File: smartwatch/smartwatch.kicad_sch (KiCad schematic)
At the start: 32 parts, among them J1 BAT_CON, J2 DC_CON, J3 PROG_INT, J4 I2C Touch, J5 SPI Display, J6 Power, J7 Micro_SD_Card, SW1 SW_Push, U1 ESP32-WROVER-E, U2 MCP73831-5-OT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

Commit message: updated pcb schematic and design
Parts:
- removed J4: I2C Touch, Connector_Wire_SMD:Wire_Pad_1x02, symbol Connector_Generic:Conn_01x02
- removed J5: SPI Display, Connector_Wire_SMD:Wire_Pad_1x03, symbol Connector_Generic:Conn_01x03
- removed J7: Micro_SD_Card, Connector_Card:microSD_HC_Hirose_DM3D-SF, symbol Connector:Micro_SD_Card
- added J4: Screen, Connector_Wire_SMD:Wire_Pad_1x07, symbol Connector_Generic:Conn_01x07
- added J5: Touch, Connector_Wire_SMD:Wire_Pad_1x04, symbol Connector_Generic:Conn_01x04
- added J8: SD Card, Connector_Wire_SMD:Wire_Pad_1x06, symbol Connector_Generic:Conn_01x06
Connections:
- net 3V3: now also J4.7 (Pin_7), J8.3 (Pin_3)
- net BTN_INP: now also U1.6 (GPIO34/ADC1_CH6); no longer U1.26 (ADC2_CH0/GPIO4)
- net GND: now also J8.5 (Pin_5)
- net SCR_MISO: now also U1.7 (GPIO35/ADC1_CH7), J4.1 (Pin_1); no longer U1.31 (GPIO19)
- net SCR_MOSI: now also J4.2 (Pin_2)
- net SCR_SCLK: now also J4.3 (Pin_3)
- net SD_MISO: now also J8.6 (Pin_6)
- net SD_MOSI: now also J8.2 (Pin_2)
- net SD_SCLK: now also J8.4 (Pin_4)
- net SD_SS: now also U1.12 (ADC2_CH7/GPIO27), J8.1 (Pin_1); no longer U1.23 (MTDO/GPIO15/ADC2_CH3)
- net TOUCH_SCL: now also J5.3 (Pin_3)
- net TOUCH_SDA: now also J5.4 (Pin_4)
- net TOUCH_IRQ: now reaches U1.10 (DAC_1/ADC2_CH8/GPIO25)
- net TOUCH_IRQ: now also J5.2 (Pin_2)
- net TOUCH_RST: now reaches U1.11 (DAC_2/ADC2_CH9/GPIO26)
- net TOUCH_RST: now also J5.1 (Pin_1)
- net SCR_CS: now reaches U1.29 (GPIO5)
- net SCR_CS: now also J4.4 (Pin_4)
- new net SCR_DC: J4.5 (Pin_5), U1.31 (GPIO19)
- new net SCR_RST: J4.6 (Pin_6), U1.23 (MTDO/GPIO15/ADC2_CH3)
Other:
- note added: "CLK"
- note added: "CMD"
- note added: "DAT0"
- note added: "DAT3"
- note added: "SD Card Interface"
- note added: "Screen Backlight"
- note added: "VDD"
- note added: "VSS"
- note removed: "HSPI SPI Interface"
- note removed: "Storage"
- note removed: "VSPI (DEFAULT) SPI Interface and default I2C"
- company: (none) -> Xonize Industries
- title: (none) -> Project Zero

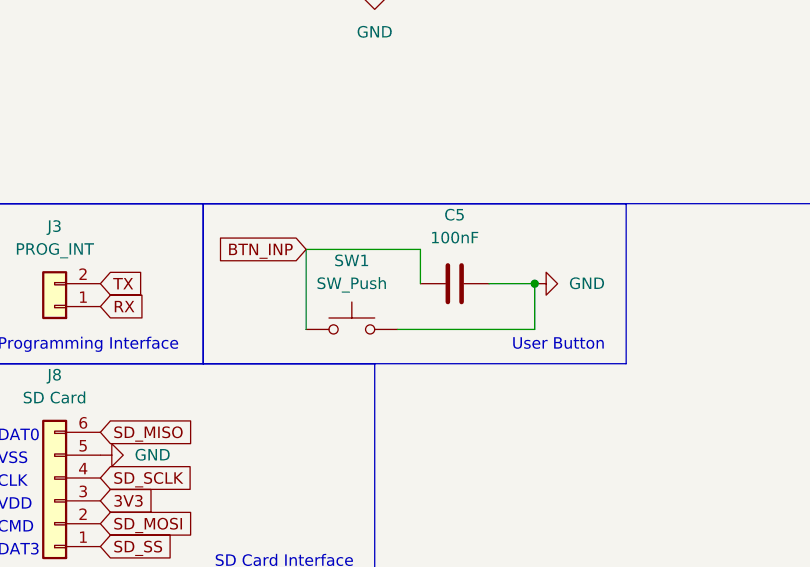
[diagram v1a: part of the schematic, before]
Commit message: changed schematic and pcb of push button connection
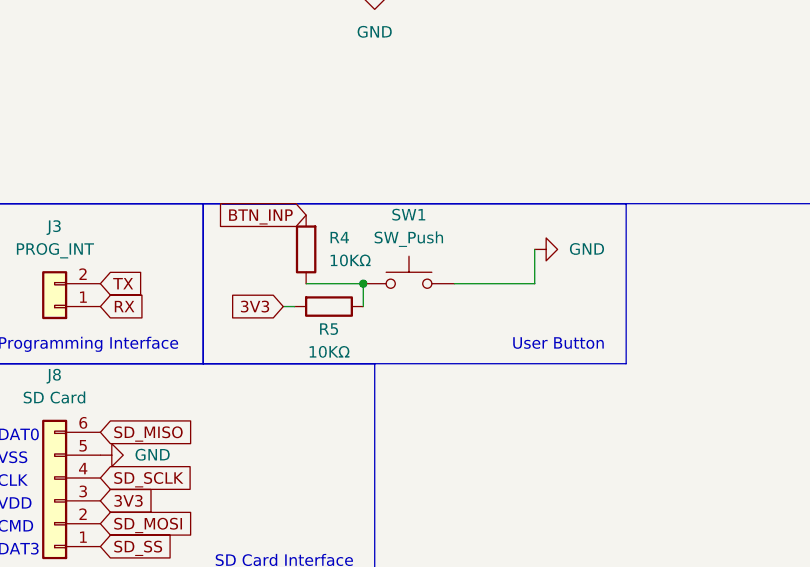
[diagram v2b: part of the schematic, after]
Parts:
- removed C5: 100nF, Capacitor_SMD:C_0805_2012Metric_Pad1.18x1.45mm_HandSolder, symbol Device:C
- added R4, R5: 10KΩ, Resistor_SMD:R_0805_2012Metric_Pad1.20x1.40mm_HandSolder, symbol Device:R
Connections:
- net 3V3: now also R5.2
- net BTN_INP: now also R4.2; no longer SW1.1
- new net: R4.1, R5.1, SW1.1
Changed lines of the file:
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@@
   (junction (at 72.39 24.13) (diameter 0) (color 0 0 0 0)
   )
-  (junction (at 177.8 110.49) (diameter 0) (color 0 0 0 0)
-  )
   (junction (at 44.45 24.13) (diameter 0) (color 0 0 0 0)
   )
@@
   (junction (at 31.75 165.1) (diameter 0) (color 0 0 0 0)
   )
+  (junction (at 158.75 110.49) (diameter 0) (color 0 0 0 0)
+  )
   (wire (pts (xy 158.75 77.47) (xy 160.02 77.47))
     (stroke (width 0) (type default))
@@
     (stroke (width 0) (type default))
   )
-  (wire (pts (xy 152.4 106.68) (xy 152.4 115.57))
-    (stroke (width 0) (type default))
-  )
   (wire (pts (xy 33.02 31.75) (xy 44.45 31.75))
     (stroke (width 0) (type default))
@@
     (stroke (width 0) (type default))
   )
-  (wire (pts (xy 165.1 110.49) (xy 165.1 106.68))
+  (wire (pts (xy 152.4 110.49) (xy 158.75 110.49))
     (stroke (width 0) (type default))
   )
@@
     (stroke (width 0) (type default))
   )
-  (wire (pts (xy 165.1 106.68) (xy 152.4 106.68))
-    (stroke (width 0) (type default))
-  )
   (wire (pts (xy 59.69 34.29) (xy 72.39 34.29))
     (stroke (width 0) (type default))
@@
     (stroke (width 0) (type default))
   )
-  (wire (pts (xy 172.72 110.49) (xy 177.8 110.49))
+  (wire (pts (xy 158.75 110.49) (xy 158.75 113.03))
+    (stroke (width 0) (type default))
+  )
+  (wire (pts (xy 177.8 110.49) (xy 177.8 106.68))
     (stroke (width 0) (type default))
   )
@@
     (stroke (width 0) (type default))
   )
+  (wire (pts (xy 149.86 113.03) (xy 151.13 113.03))
+    (stroke (width 0) (type default))
+  )
+  (wire (pts (xy 168.91 110.49) (xy 177.8 110.49))
+    (stroke (width 0) (type default))
+  )
   (wire (pts (xy 50.8 52.07) (xy 50.8 54.61))
     (stroke (width 0) (type default))
@@
     (stroke (width 0) (type default))
   )
-  (wire (pts (xy 162.56 115.57) (xy 177.8 115.57))
-    (stroke (width 0) (type default))
-  )
   (wire (pts (xy 40.64 57.15) (xy 45.72 57.15))
     (stroke (width 0) (type default))
@@
   )
   (wire (pts (xy 45.72 135.89) (xy 25.4 135.89))
-    (stroke (width 0) (type default))
-  )
-  (wire (pts (xy 177.8 115.57) (xy 177.8 110.49))
     (stroke (width 0) (type default))
   )
@@
     )
   )
+  (global_label "3V3" (shape input) (at 149.86 113.03 180) (fields_autoplaced)
+    (effects (font (size 1.27 1.27)) (justify right))
+    (property "Intersheetrefs" "${INTERSHEET_REFS}" (at 143.4466 113.03 0)
+      (effects (font (size 1.27 1.27)) (justify right) hide)
+    )
+  )
   (global_label "TOUCH_IRQ" (shape input) (at 194.31 66.04 0) (fields_autoplaced)
     (effects (font (size 1.27 1.27)) (justify left))
@@
     )
   )
+  (global_label "BTN_INP" (shape input) (at 152.4 102.87 180) (fields_autoplaced)
+    (effects (font (size 1.27 1.27)) (justify right))
+    (property "Intersheetrefs" "${INTERSHEET_REFS}" (at 141.7532 102.87 0)
+      (effects (font (size 1.27 1.27)) (justify right) hide)
+    )
+  )
   (global_label "3V3" (shape input) (at 158.75 30.48 90) (fields_autoplaced)
     (effects (font (size 1.27 1.27)) (justify left))
@@
     (effects (font (size 1.27 1.27)) (justify right))
     (property "Intersheetrefs" "${INTERSHEET_REFS}" (at 112.5432 60.96 0)
-      (effects (font (size 1.27 1.27)) (justify right) hide)
-    )
-  )
-  (global_label "BTN_INP" (shape input) (at 152.4 106.68 180) (fields_autoplaced)
-    (effects (font (size 1.27 1.27)) (justify right))
-    (property "Intersheetrefs" "${INTERSHEET_REFS}" (at 141.7532 106.68 0)
       (effects (font (size 1.27 1.27)) (justify right) hide)
     )
@@
         (path "/ed763a40-a5bc-4ad5-80fd-af92dd7e1451"
           (reference "#PWR07") (unit 1)
-        )
-      )
-    )
-  )
-  (symbol (lib_id "power:GND") (at 177.8 110.49 90) (unit 1)
-    (in_bom yes) (on_board yes) (dnp no) (fields_autoplaced)
-    (property "Reference" "#PWR016" (at 184.15 110.49 0)
-      (effects (font (size 1.27 1.27)) hide)
-    )
-    (property "Value" "GND" (at 181.61 110.49 90)
-      (effects (font (size 1.27 1.27)) (justify right))
-    )
-    (property "Footprint" "" (at 177.8 110.49 0)
-      (effects (font (size 1.27 1.27)) hide)
-    )
-    (property "Datasheet" "" (at 177.8 110.49 0)
-      (effects (font (size 1.27 1.27)) hide)
-    )
-    (pin "1")
-    (instances
-      (project "smartwatch"
-        (path "/ed763a40-a5bc-4ad5-80fd-af92dd7e1451"
-          (reference "#PWR016") (unit 1)
         )
       )
@@
     )
   )
+  (symbol (lib_id "power:GND") (at 177.8 106.68 90) (unit 1)
+    (in_bom yes) (on_board yes) (dnp no) (fields_autoplaced)
+    (property "Reference" "#PWR014" (at 184.15 106.68 0)
+      (effects (font (size 1.27 1.27)) hide)
+    )
+    (property "Value" "GND" (at 181.61 106.68 90)
+      (effects (font (size 1.27 1.27)) (justify right))
+    )
+    (property "Footprint" "" (at 177.8 106.68 0)
+      (effects (font (size 1.27 1.27)) hide)
+    )
+    (property "Datasheet" "" (at 177.8 106.68 0)
+      (effects (font (size 1.27 1.27)) hide)
+    )
+    (pin "1")
+    (instances
+      (project "smartwatch"
+        (path "/ed763a40-a5bc-4ad5-80fd-af92dd7e1451"
+          (reference "#PWR014") (unit 1)
+        )
+      )
+    )
+  )
   (symbol (lib_id "power:GND") (at 129.54 129.54 90) (unit 1)
     (in_bom yes) (on_board yes) (dnp no) (fields_autoplaced)
@@
         (path "/ed763a40-a5bc-4ad5-80fd-af92dd7e1451"
           (reference "J1") (unit 1)
+        )
+      )
+    )
+  )
+  (symbol (lib_id "Switch:SW_Push") (at 163.83 110.49 0) (unit 1)
+    (in_bom yes) (on_board yes) (dnp no) (fields_autoplaced)
+    (property "Reference" "SW1" (at 163.83 102.87 0)
+      (effects (font (size 1.27 1.27)))
+    )
+    (property "Value" "SW_Push" (at 163.83 105.41 0)
+      (effects (font (size 1.27 1.27)))
+    )
+    (property "Footprint" "Side_Button:Wurth_Elektronik_436331045822" (at 163.83 105.41 0)
+      (effects (font (size 1.27 1.27)) hide)
+    )
+    (property "Datasheet" "~" (at 163.83 105.41 0)
+      (effects (font (size 1.27 1.27)) hide)
+    )
+    (pin "1")
+    (pin "2")
+    (instances
+      (project "smartwatch"
+        (path "/ed763a40-a5bc-4ad5-80fd-af92dd7e1451"
+          (reference "SW1") (unit 1)
+        )
+      )
+    )
+  )
+  (symbol (lib_id "Device:R") (at 154.94 113.03 270) (unit 1)
+    (in_bom yes) (on_board yes) (dnp no)
+    (property "Reference" "R5" (at 154.94 115.57 90)
+      (effects (font (size 1.27 1.27)))
+    )
+    (property "Value" "10KΩ" (at 154.94 118.11 90)
+      (effects (font (size 1.27 1.27)))
+    )
+    (property "Footprint" "Resistor_SMD:R_0805_2012Metric_Pad1.20x1.40mm_HandSolder" (at 154.94 111.252 90)
+      (effects (font (size 1.27 1.27)) hide)
+    )
+    (property "Datasheet" "~" (at 154.94 113.03 0)
+      (effects (font (size 1.27 1.27)) hide)
+    )
+    (pin "1")
+    (pin "2")
+    (instances
+      (project "smartwatch"
+        (path "/ed763a40-a5bc-4ad5-80fd-af92dd7e1451"
+          (reference "R5") (unit 1)
         )
       )
@@
     )
   )
-  (symbol (lib_id "Switch:SW_Push") (at 157.48 115.57 0) (unit 1)
-    (in_bom yes) (on_board yes) (dnp no) (fields_autoplaced)
-    (property "Reference" "SW1" (at 157.48 107.95 0)
-      (effects (font (size 1.27 1.27)))
-    )
-    (property "Value" "SW_Push" (at 157.48 110.49 0)
-      (effects (font (size 1.27 1.27)))
-    )
-    (property "Footprint" "Side_Button:Wurth_Elektronik_436331045822" (at 157.48 110.49 0)
-      (effects (font (size 1.27 1.27)) hide)
-    )
-    (property "Datasheet" "~" (at 157.48 110.49 0)
-      (effects (font (size 1.27 1.27)) hide)
-    )
-    (pin "1")
-    (pin "2")
-    (instances
-      (project "smartwatch"
-        (path "/ed763a40-a5bc-4ad5-80fd-af92dd7e1451"
-          (reference "SW1") (unit 1)
-        )
-      )
-    )
-  )
   (symbol (lib_id "power:GND") (at 59.69 118.11 90) (unit 1)
     (in_bom yes) (on_board yes) (dnp no) (fields_autoplaced)
@@
     )
   )
-  (symbol (lib_id "Device:C") (at 168.91 110.49 270) (unit 1)
-    (in_bom yes) (on_board yes) (dnp no) (fields_autoplaced)
-    (property "Reference" "C5" (at 168.91 102.87 90)
-      (effects (font (size 1.27 1.27)))
-    )
-    (property "Value" "100nF" (at 168.91 105.41 90)
-      (effects (font (size 1.27 1.27)))
-    )
-    (property "Footprint" "Capacitor_SMD:C_0805_2012Metric_Pad1.18x1.45mm_HandSolder" (at 165.1 111.4552 0)
-      (effects (font (size 1.27 1.27)) hide)
-    )
-    (property "Datasheet" "~" (at 168.91 110.49 0)
-      (effects (font (size 1.27 1.27)) hide)
-    )
-    (pin "1")
-    (pin "2")
-    (instances
-      (project "dbv2"
-        (path "/968668d6-4dbf-4f5c-bf30-54339806b473"
-          (reference "C5") (unit 1)
-        )
-      )
-      (project "smartwatch"
-        (path "/ed763a40-a5bc-4ad5-80fd-af92dd7e1451"
-          (reference "C13") (unit 1)
-        )
-      )
+  (symbol (lib_id "Device:R") (at 152.4 106.68 180) (unit 1)
+    (in_bom yes) (on_board yes) (dnp no) (fields_autoplaced)
+    (property "Reference" "R4" (at 154.94 105.41 0)
+      (effects (font (size 1.27 1.27)) (justify right))
+    )
+    (property "Value" "10KΩ" (at 154.94 107.95 0)
+      (effects (font (size 1.27 1.27)) (justify right))
+    )
+    (property "Footprint" "Resistor_SMD:R_0805_2012Metric_Pad1.20x1.40mm_HandSolder" (at 154.178 106.68 90)
+      (effects (font (size 1.27 1.27)) hide)
+    )
+    (property "Datasheet" "~" (at 152.4 106.68 0)
+      (effects (font (size 1.27 1.27)) hide)
+    )
+    (pin "1")
+    (pin "2")
+    (instances
+      (project "smartwatch"
+        (path "/ed763a40-a5bc-4ad5-80fd-af92dd7e1451"
+          (reference "R4") (unit 1)
+        )
+      )

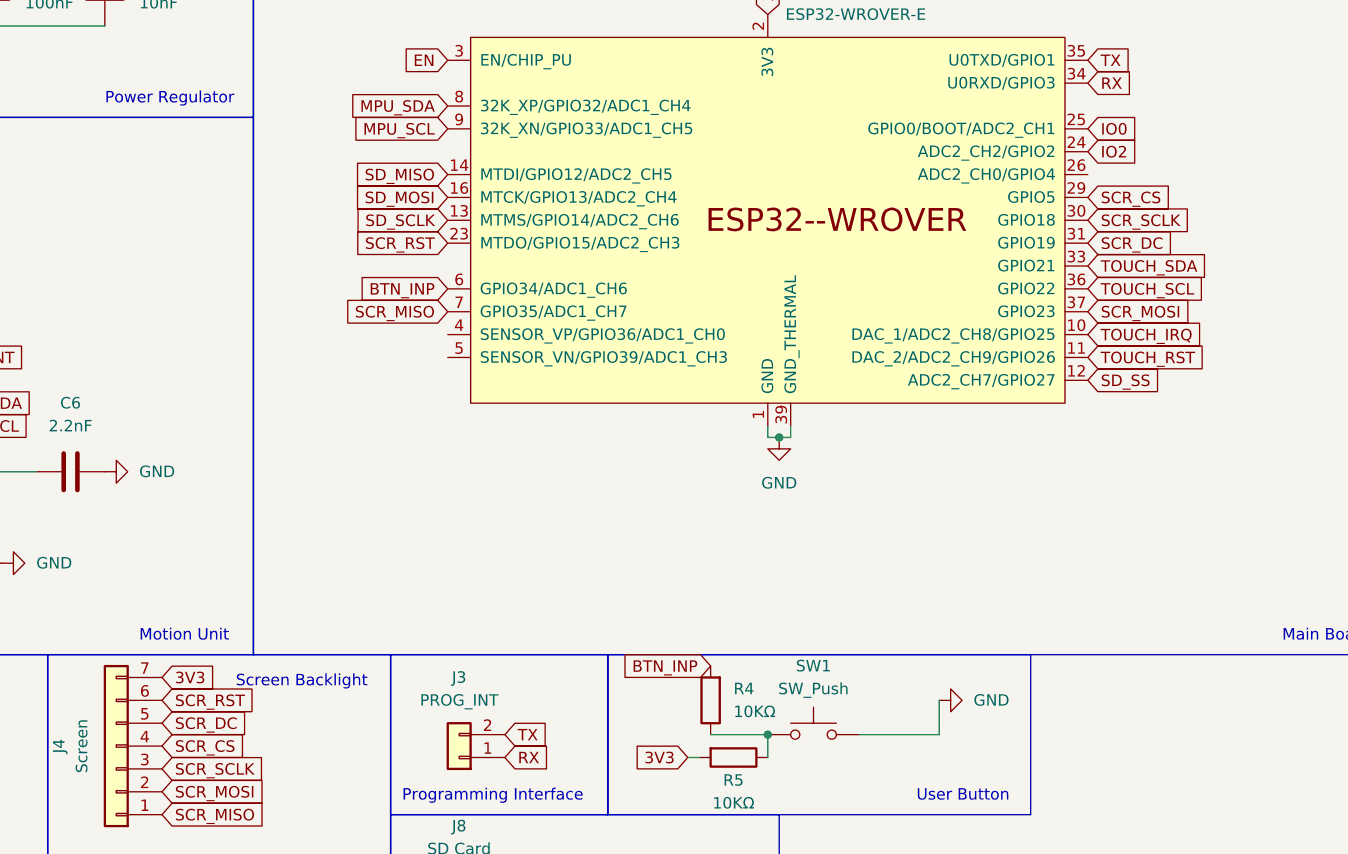
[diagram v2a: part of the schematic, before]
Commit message: backlight toggling, stepcount ring
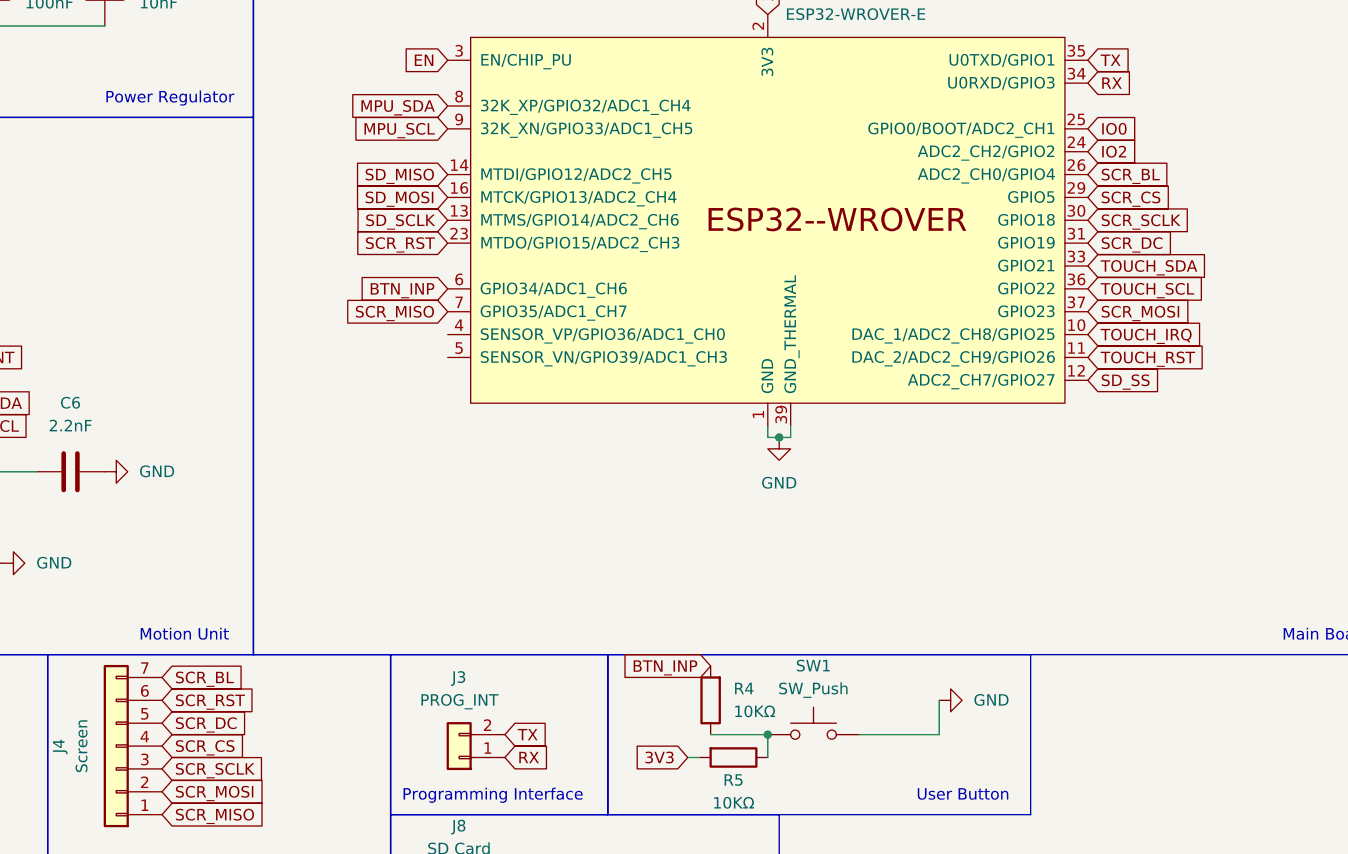
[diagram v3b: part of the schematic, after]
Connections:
- net 3V3: no longer J4.7 (Pin_7)
- net SCR_BL: now reaches U1.26 (ADC2_CH0/GPIO4)
- net SCR_BL: now also J4.7 (Pin_7)
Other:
- note removed: "Screen Backlight"
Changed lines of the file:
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@@
     (effects (font (size 1.27 1.27)) (justify left bottom))
-  )
-  (text "Screen Backlight" (at 114.3 105.41 0)
-    (effects (font (size 1.27 1.27)) (justify right bottom))
   )
   (text "User Button" (at 175.26 118.11 0)
@@
     )
   )
+  (global_label "SCR_BL" (shape input) (at 194.31 48.26 0) (fields_autoplaced)
+    (effects (font (size 1.27 1.27)) (justify left))
+    (property "Intersheetrefs" "${INTERSHEET_REFS}" (at 204.231 48.26 0)
+      (effects (font (size 1.27 1.27)) (justify left) hide)
+    )
+  )
   (global_label "RX" (shape input) (at 129.54 113.03 0) (fields_autoplaced)
     (effects (font (size 1.27 1.27)) (justify left))
@@
     )
   )
+  (global_label "SCR_BL" (shape input) (at 91.44 104.14 0) (fields_autoplaced)
+    (effects (font (size 1.27 1.27)) (justify left))
+    (property "Intersheetrefs" "${INTERSHEET_REFS}" (at 101.361 104.14 0)
+      (effects (font (size 1.27 1.27)) (justify left) hide)
+    )
+  )
   (global_label "SD_SS" (shape input) (at 194.31 71.12 0) (fields_autoplaced)
     (effects (font (size 1.27 1.27)) (justify left))
@@
       (effects (font (size 1.27 1.27)) (justify left) hide)
     )
-  )
-  (global_label "3V3" (shape input) (at 91.44 104.14 0) (fields_autoplaced)
-    (effects (font (size 1.27 1.27)) (justify left))
-    (property "Intersheetrefs" "${INTERSHEET_REFS}" (at 97.8534 104.14 0)
-      (effects (font (size 1.27 1.27)) (justify left) hide)
-    )
